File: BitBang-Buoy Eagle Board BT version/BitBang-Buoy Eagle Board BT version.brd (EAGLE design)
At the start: 81.3 x 84.8 mm, 20 parts, among them IC1 7805TV

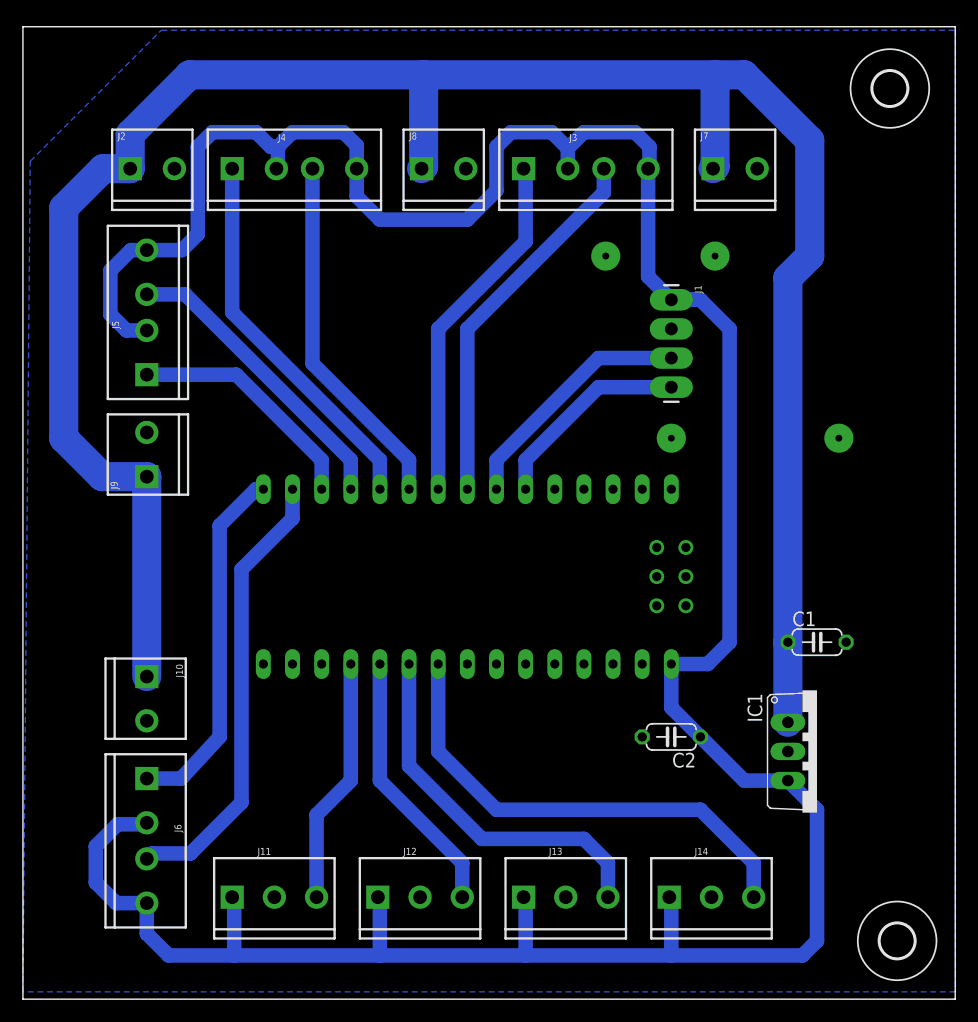
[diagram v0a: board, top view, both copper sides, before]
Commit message: New pinout adapted
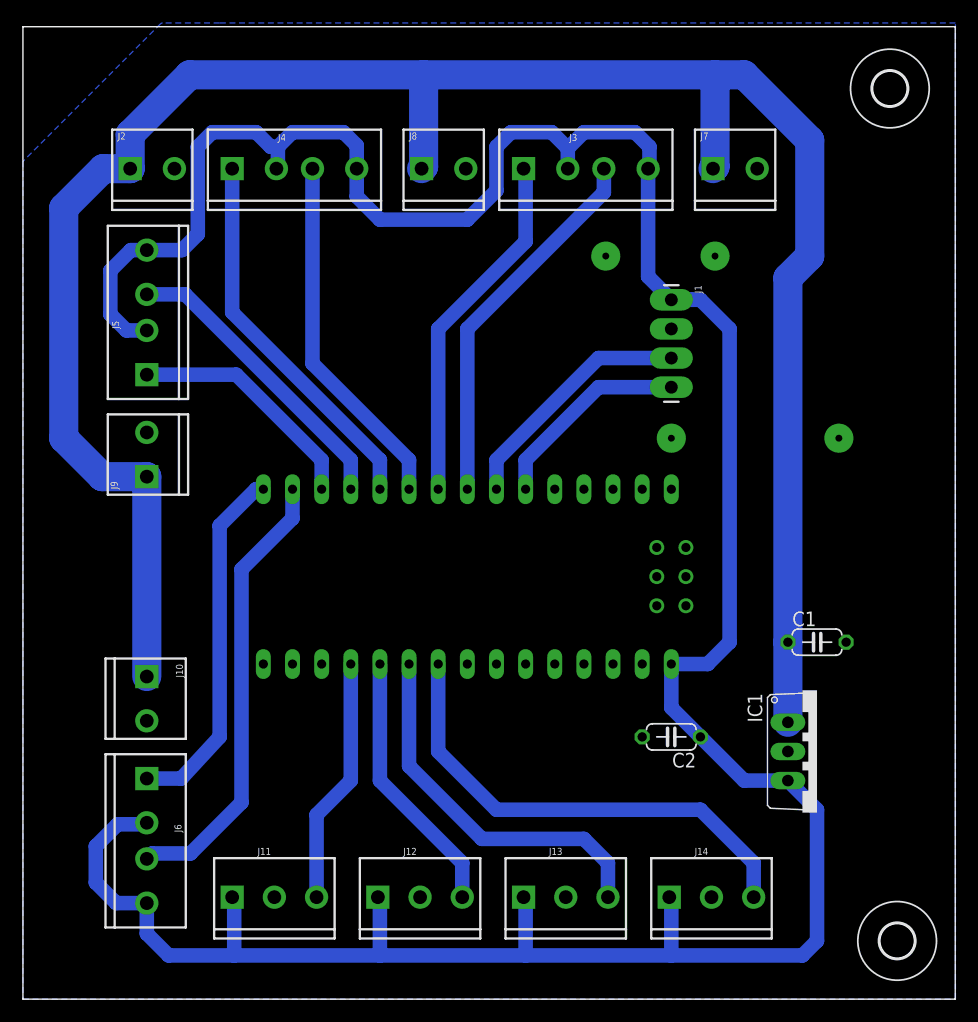
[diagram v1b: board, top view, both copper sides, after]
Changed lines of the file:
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@@
 <layer number="27" name="tValues" color="7" fill="1" visible="yes" active="yes"/>
 <layer number="28" name="bValues" color="7" fill="1" visible="yes" active="yes"/>
-<layer number="29" name="tStop" color="7" fill="3" visible="no" active="yes"/>
-<layer number="30" name="bStop" color="7" fill="6" visible="no" active="yes"/>
-<layer number="31" name="tCream" color="7" fill="4" visible="no" active="yes"/>
-<layer number="32" name="bCream" color="7" fill="5" visible="no" active="yes"/>
-<layer number="33" name="tFinish" color="6" fill="3" visible="no" active="yes"/>
-<layer number="34" name="bFinish" color="6" fill="6" visible="no" active="yes"/>
-<layer number="35" name="tGlue" color="7" fill="4" visible="no" active="yes"/>
-<layer number="36" name="bGlue" color="7" fill="5" visible="no" active="yes"/>
-<layer number="37" name="tTest" color="7" fill="1" visible="no" active="yes"/>
-<layer number="38" name="bTest" color="7" fill="1" visible="no" active="yes"/>
+<layer number="29" name="tStop" color="7" fill="3" visible="yes" active="yes"/>
+<layer number="30" name="bStop" color="7" fill="6" visible="yes" active="yes"/>
+<layer number="31" name="tCream" color="7" fill="4" visible="yes" active="yes"/>
+<layer number="32" name="bCream" color="7" fill="5" visible="yes" active="yes"/>
+<layer number="33" name="tFinish" color="6" fill="3" visible="yes" active="yes"/>
+<layer number="34" name="bFinish" color="6" fill="6" visible="yes" active="yes"/>
+<layer number="35" name="tGlue" color="7" fill="4" visible="yes" active="yes"/>
+<layer number="36" name="bGlue" color="7" fill="5" visible="yes" active="yes"/>
+<layer number="37" name="tTest" color="7" fill="1" visible="yes" active="yes"/>
+<layer number="38" name="bTest" color="7" fill="1" visible="yes" active="yes"/>
 <layer number="39" name="tKeepout" color="4" fill="11" visible="yes" active="yes"/>
 <layer number="40" name="bKeepout" color="1" fill="11" visible="yes" active="yes"/>
@@
 <layer number="42" name="bRestrict" color="1" fill="10" visible="yes" active="yes"/>
 <layer number="43" name="vRestrict" color="2" fill="10" visible="yes" active="yes"/>
-<layer number="44" name="Drills" color="7" fill="1" visible="no" active="yes"/>
-<layer number="45" name="Holes" color="7" fill="1" visible="no" active="yes"/>
-<layer number="46" name="Milling" color="3" fill="1" visible="no" active="yes"/>
+<layer number="44" name="Drills" color="7" fill="1" visible="yes" active="yes"/>
+<layer number="45" name="Holes" color="7" fill="1" visible="yes" active="yes"/>
+<layer number="46" name="Milling" color="3" fill="1" visible="yes" active="yes"/>
 <layer number="47" name="Measures" color="7" fill="1" visible="yes" active="yes"/>
 <layer number="48" name="Document" color="7" fill="1" visible="yes" active="yes"/>
@@
 <contactref element="J12" pad="2"/>
 <contactref element="J11" pad="2"/>
-<polygon width="0.6096" layer="16" spacing="0.6096" isolate="0.6096" orphans="yes" thermals="no">
-<vertex x="6.35" y="79.375"/>
+<via x="50.8" y="43.815" extent="1-16" drill="0.6" diameter="2.54"/>
+<via x="65.405" y="43.815" extent="1-16" drill="0.6" diameter="2.54"/>
+<via x="45.085" y="59.69" extent="1-16" drill="0.6" diameter="2.54"/>
+<via x="54.61" y="59.69" extent="1-16" drill="0.6" diameter="2.54"/>
+<polygon width="0.4064" layer="16" spacing="0.254" isolate="0.6096" orphans="yes">
+<vertex x="-5.715" y="-5.08"/>
+<vertex x="75.565" y="-5.08"/>
 <vertex x="75.565" y="79.375"/>
-<vertex x="75.565" y="-4.445"/>
-<vertex x="-5.715" y="-4.445"/>
-<vertex x="-5.08" y="67.945"/>
+<vertex x="75.565" y="80.01"/>
+<vertex x="11.43" y="80.01"/>
+<vertex x="6.455209375" y="80.01" curve="44.999502"/>
+<vertex x="6.27560625" y="79.93560625"/>
+<vertex x="-5.715" y="67.945"/>
 </polygon>
-<wire x1="48.26" y1="17.78" x2="60.96" y2="16.51" width="0" layer="19" extent="1-1"/>
+<wire x1="50.8" y1="53.34" x2="54.61" y2="59.69" width="0" layer="19" extent="1-1"/>
 </signal>
 <signal name="N$4">
@@
 <wire x1="53.34" y1="11.43" x2="57.9778" y2="6.7922" width="1.27" layer="16"/>
 </signal>
-<signal name="N$1">
-<via x="50.8" y="43.815" extent="1-16" drill="0.6" diameter="2.54"/>
-</signal>
-<signal name="N$2">
-<via x="65.405" y="43.815" extent="1-16" drill="0.6" diameter="2.54"/>
-</signal>
-<signal name="N$3">
-<via x="45.085" y="59.69" extent="1-16" drill="0.6" diameter="2.54"/>
-</signal>
-<signal name="N$18">
-<via x="54.61" y="59.69" extent="1-16" drill="0.6" diameter="2.54"/>
-</signal>
 </signals>
